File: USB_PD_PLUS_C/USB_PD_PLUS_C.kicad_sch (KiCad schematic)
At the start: 28 parts, among them J1 USB3_A, U1 NDP1360KC, U3 CH482D, U4 CXP0650-220M-AG(22UH), U5 LM317L_SOT-89

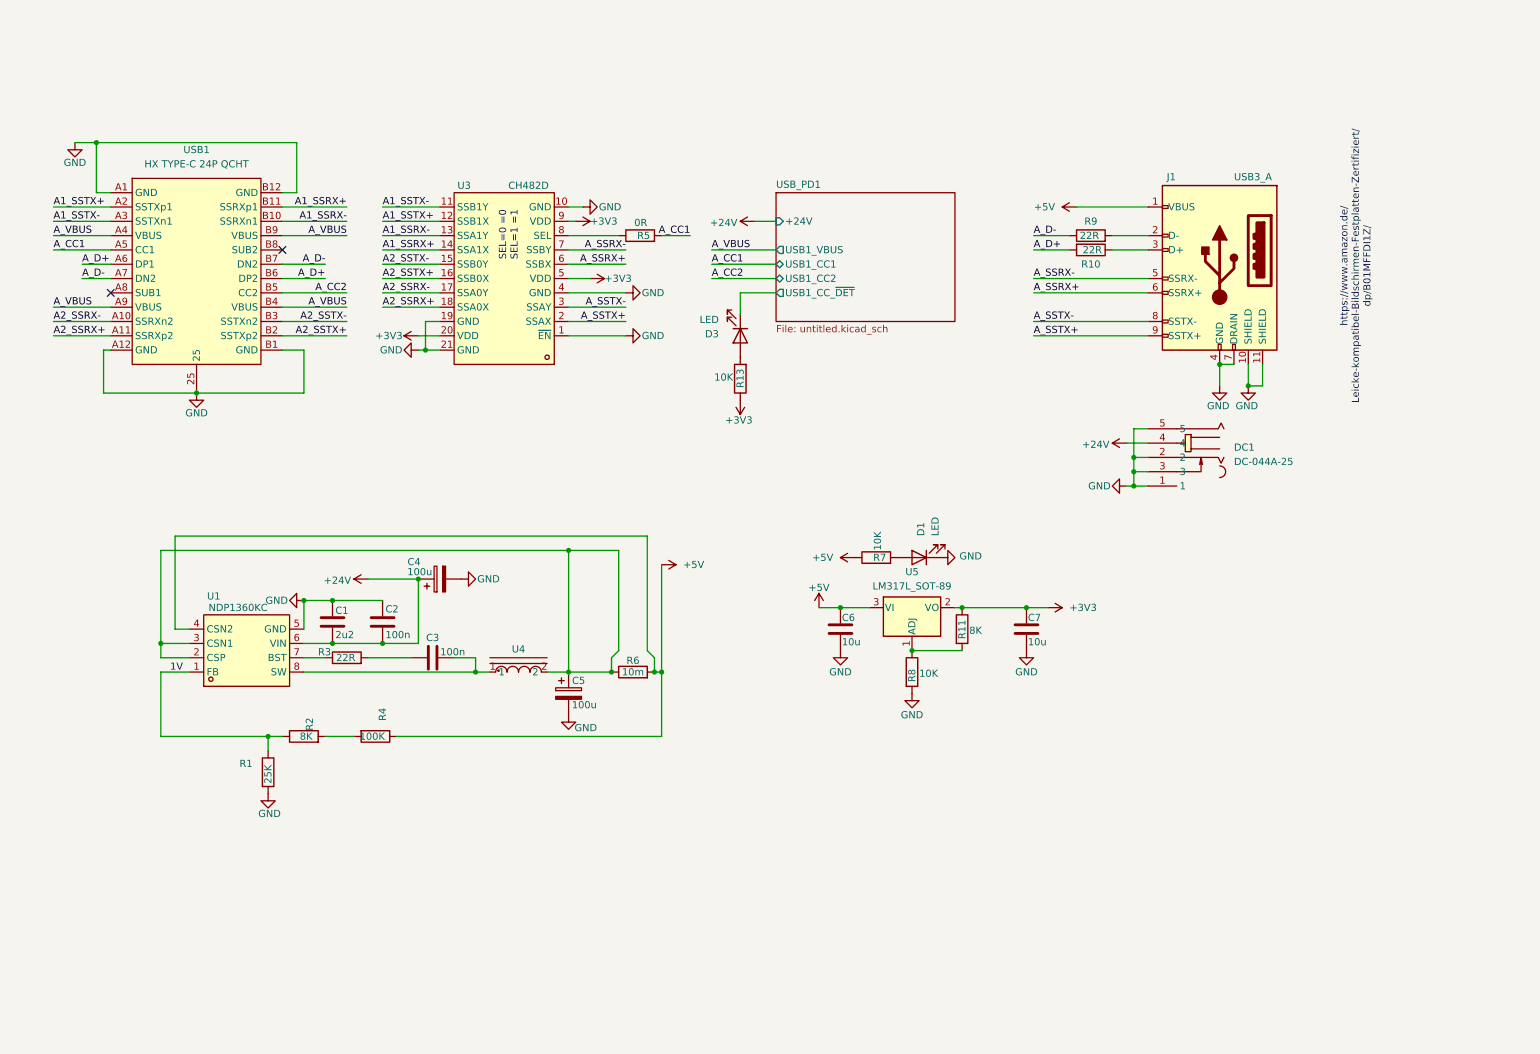
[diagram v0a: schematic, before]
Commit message: Update Schematic to 3 Port USB-C Power
I updated the schamtic to 3 port usb-C with superspeed and PD working
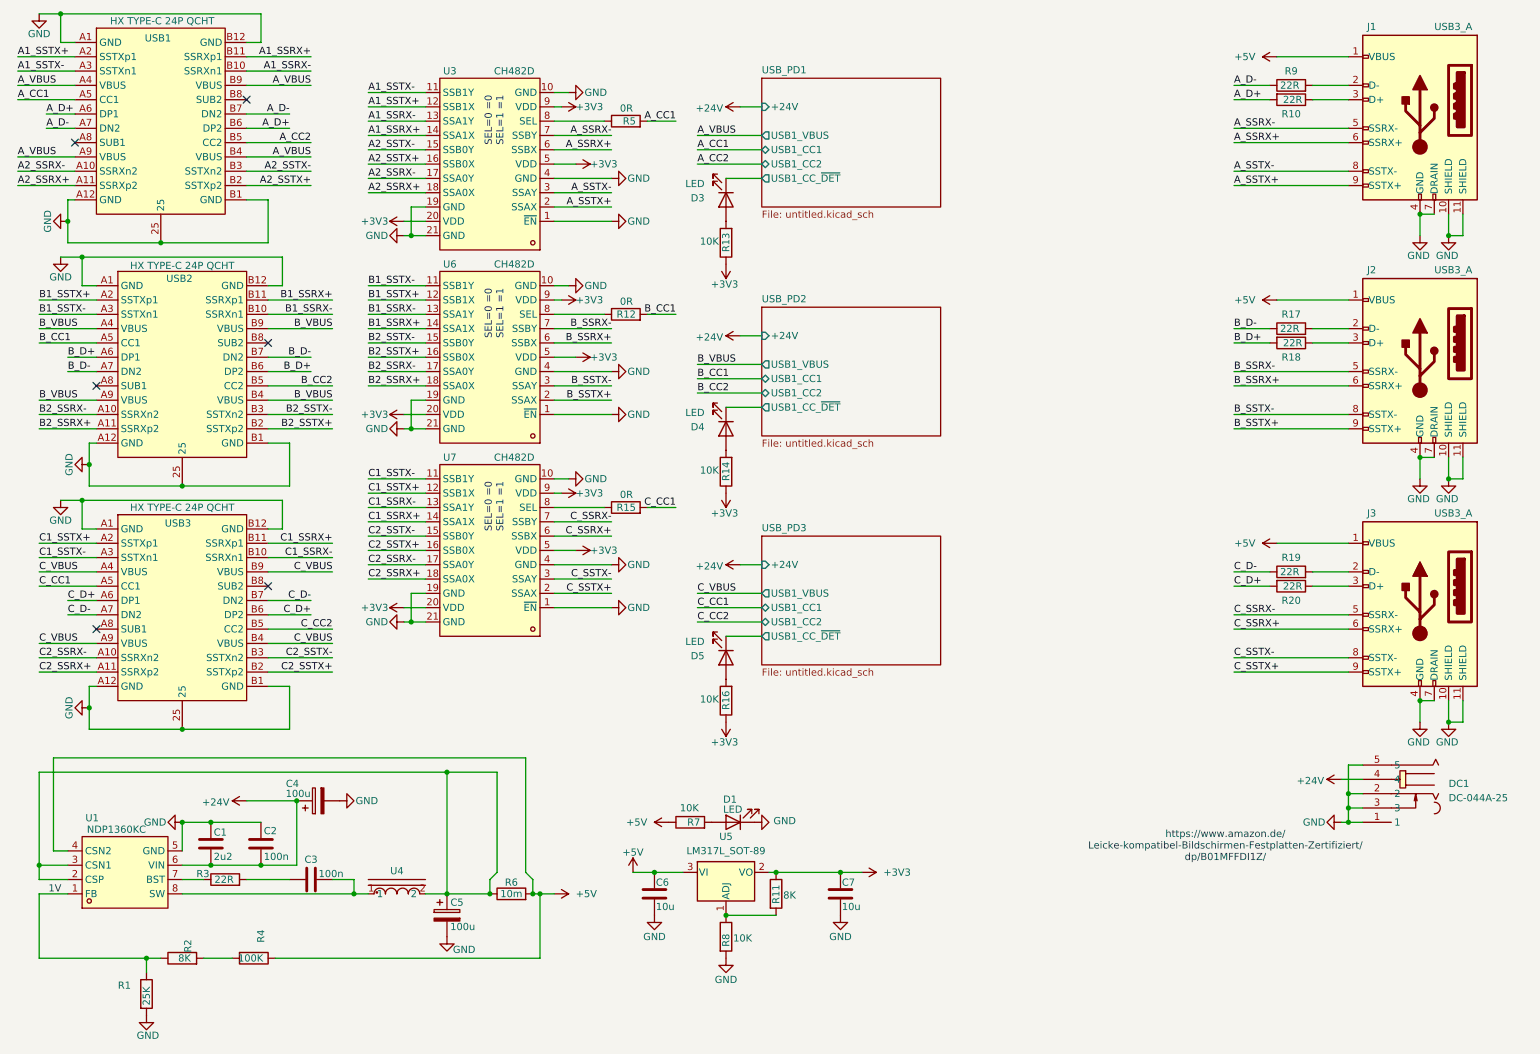
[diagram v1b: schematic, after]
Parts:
- added D4, D5: LED, LED_SMD:LED_0603_1608Metric, symbol Device:LED
- added J2, J3: USB3_A, easyeda2kicad:USB-3.0-A-TH_HC-ST-003-01-Z, symbol Connector:USB3_A
- added R12, R15: 0R, Resistor_SMD:R_0402_1005Metric, symbol Device:R
- added R14, R16: 10K, Resistor_SMD:R_0402_1005Metric, symbol Device:R
- added R17, R18, R19, R20: 22R, Resistor_SMD:R_0402_1005Metric, symbol Device:R
- added U6, U7: CH482D, easyeda2kicad:VFQFN-20_L4.5-W2.5-P0.5-BL-EP, symbol EASYEDA:CH482D
- added USB2, USB3: HX TYPE-C 24P QCHT, easyeda2kicad:TYPE-C-SMD_TYPE-C-24P-QCHT, symbol EASYEDA:HXTYPE-C24PQCHT
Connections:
- net +3V3: now also R14.1, R16.1, U6.20 (VDD), U6.5 (VDD), U6.9 (VDD), U7.20 (VDD), U7.5 (VDD), U7.9 (VDD)
- net +5V: now also J2.1 (VBUS), J3.1 (VBUS)
- net GND: now also J2.10 (SHIELD), J2.11 (SHIELD), J2.4 (GND), J2.7 (DRAIN), J3.10 (SHIELD), J3.11 (SHIELD), J3.4 (GND), J3.7 (DRAIN), U6.1 (~{EN}), U6.10 (GND), U6.19 (GND), U6.21 (GND), U6.4 (GND), U7.1 (~{EN}), U7.10 (GND), U7.19 (GND), U7.21 (GND), U7.4 (GND), USB2.25, USB2.A1 (GND), USB2.A12 (GND), USB2.B1 (GND), USB2.B12 (GND), USB3.25, USB3.A1 (GND), USB3.A12 (GND), USB3.B1 (GND), USB3.B12 (GND)
- new net: R15.1, U7.8 (SEL)
- new net: D5.2 (A), R16.2
- new net: R12.1, U6.8 (SEL)
- new net: J2.3 (D+), R18.1
- new net: D4.2 (A), R14.2
- new net: J3.2 (D-), R19.2
- new net: J3.3 (D+), R20.1
- new net: J2.2 (D-), R17.2
- new net B1_SSRX+: U6.14 (SSA1X), USB2.B11 (SSRXp1)
- new net B1_SSRX-: U6.13 (SSA1Y), USB2.B10 (SSRXn1)
- new net B1_SSTX+: U6.12 (SSB1X), USB2.A2 (SSTXp1)
- new net B1_SSTX-: U6.11 (SSB1Y), USB2.A3 (SSTXn1)
- new net B2_SSRX+: U6.18 (SSA0X), USB2.A11 (SSRXp2)
- new net B2_SSRX-: U6.17 (SSA0Y), USB2.A10 (SSRXn2)
- new net B2_SSTX+: U6.16 (SSB0X), USB2.B2 (SSTXp2)
- new net B2_SSTX-: U6.15 (SSB0Y), USB2.B3 (SSTXn2)
- new net B_CC1: R12.2, USB2.A5 (CC1)
- new net B_CC2: USB2.B5 (CC2)
- new net B_D+: R18.2, USB2.A6 (DP1), USB2.B6 (DP2)
- new net B_D-: R17.1, USB2.A7 (DN2), USB2.B7 (DN2)
- new net B_SSRX+: J2.6 (SSRX+), U6.6 (SSBX)
- new net B_SSRX-: J2.5 (SSRX-), U6.7 (SSBY)
- new net B_SSTX+: J2.9 (SSTX+), U6.2 (SSAX)
- new net B_SSTX-: J2.8 (SSTX-), U6.3 (SSAY)
- new net B_VBUS: USB2.A4 (VBUS), USB2.A9 (VBUS), USB2.B4 (VBUS), USB2.B9 (VBUS)
- new net C1_SSRX+: U7.14 (SSA1X), USB3.B11 (SSRXp1)
- new net C1_SSRX-: U7.13 (SSA1Y), USB3.B10 (SSRXn1)
- new net C1_SSTX+: U7.12 (SSB1X), USB3.A2 (SSTXp1)
- new net C1_SSTX-: U7.11 (SSB1Y), USB3.A3 (SSTXn1)
- new net C2_SSRX+: U7.18 (SSA0X), USB3.A11 (SSRXp2)
- new net C2_SSRX-: U7.17 (SSA0Y), USB3.A10 (SSRXn2)
- new net C2_SSTX+: U7.16 (SSB0X), USB3.B2 (SSTXp2)
- new net C2_SSTX-: U7.15 (SSB0Y), USB3.B3 (SSTXn2)
- new net C_CC1: R15.2, USB3.A5 (CC1)
- new net C_CC2: USB3.B5 (CC2)
- new net C_D+: R20.2, USB3.A6 (DP1), USB3.B6 (DP2)
- new net C_D-: R19.1, USB3.A7 (DN2), USB3.B7 (DN2)
- new net C_SSRX+: J3.6 (SSRX+), U7.6 (SSBX)
- new net C_SSRX-: J3.5 (SSRX-), U7.7 (SSBY)
- new net C_SSTX+: J3.9 (SSTX+), U7.2 (SSAX)
- new net C_SSTX-: J3.8 (SSTX-), U7.3 (SSAY)
- new net C_VBUS: USB3.A4 (VBUS), USB3.A9 (VBUS), USB3.B4 (VBUS), USB3.B9 (VBUS)
- new net USB_PD2/USB1_CC_~{DET}: D4.1 (K)
- new net USB_PD3/USB1_CC_~{DET}: D5.1 (K)
- no-connect marks 2 -> 6
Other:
- added sheet USB_PD2 (untitled.kicad_sch)
- added sheet USB_PD3 (untitled.kicad_sch)
- moved on the sheet: C1, C2, C3, C4, C5, C6, C7, D1, D3, DC1, J1, R1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

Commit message: update USB PD PCB to 3 in 3 out
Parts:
- removed C1: 2u2, easyeda2kicad:C1812, symbol Device:C
- removed C4, C5: 100u, Capacitor_SMD:CP_Elec_8x10, symbol Device:C_Polarized
- added C16, C9: 22u, easyeda2kicad:C1812, symbol Device:C
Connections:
- net +24V: now also C16.1
- net GND: now also C16.2, C9.2
- net at R6.1, U1.2 (CSP), U1.3 (CSN1)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: now also C9.1
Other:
- moved on the sheet: C2

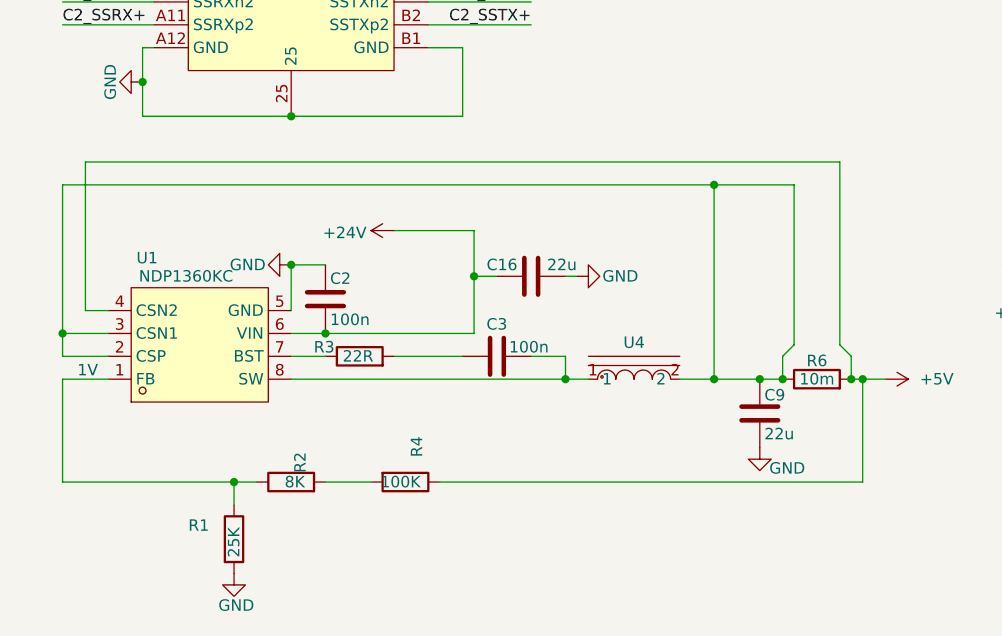
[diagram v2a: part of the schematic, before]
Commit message: update routing usb c pd
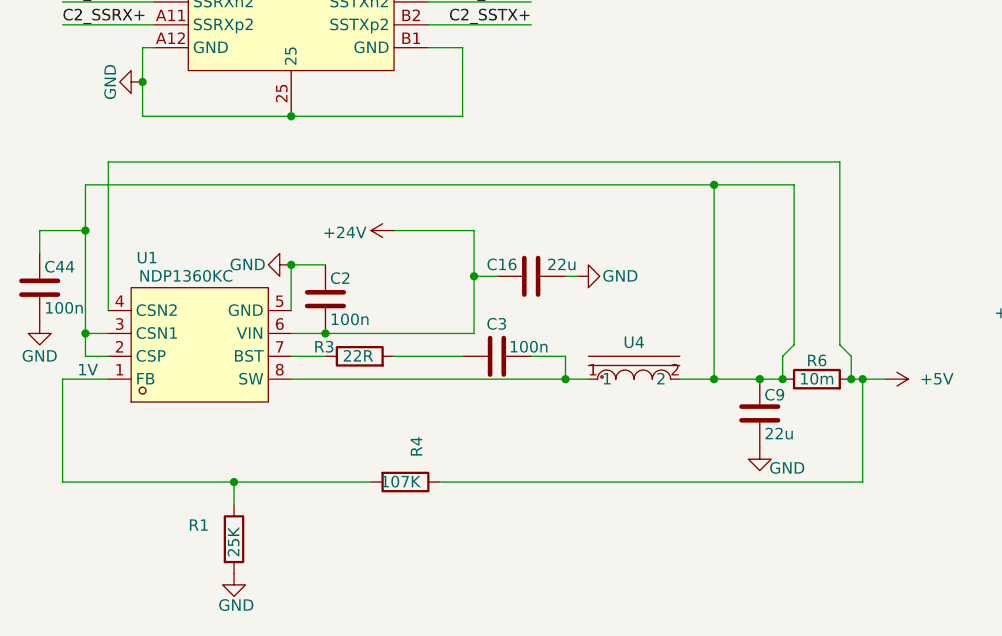
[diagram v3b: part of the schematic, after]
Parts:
- removed R2: 8K, Resistor_SMD:R_0402_1005Metric, symbol Device:R
- added C44: 100n, Capacitor_SMD:C_0402_1005Metric, symbol Device:C
- C2, C3: footprint Capacitor_SMD:C_0603_1608Metric -> Capacitor_SMD:C_0402_1005Metric; LCSC C5137636 -> C5142567
- R4: value 100K -> 107K; LCSC Part C3017514 -> C25743
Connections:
- net GND: now also C44.2
- net at R1.1, U1.1 (FB): now also R4.2
- net at C9.1, R6.1, U1.2 (CSP)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: now also C44.1

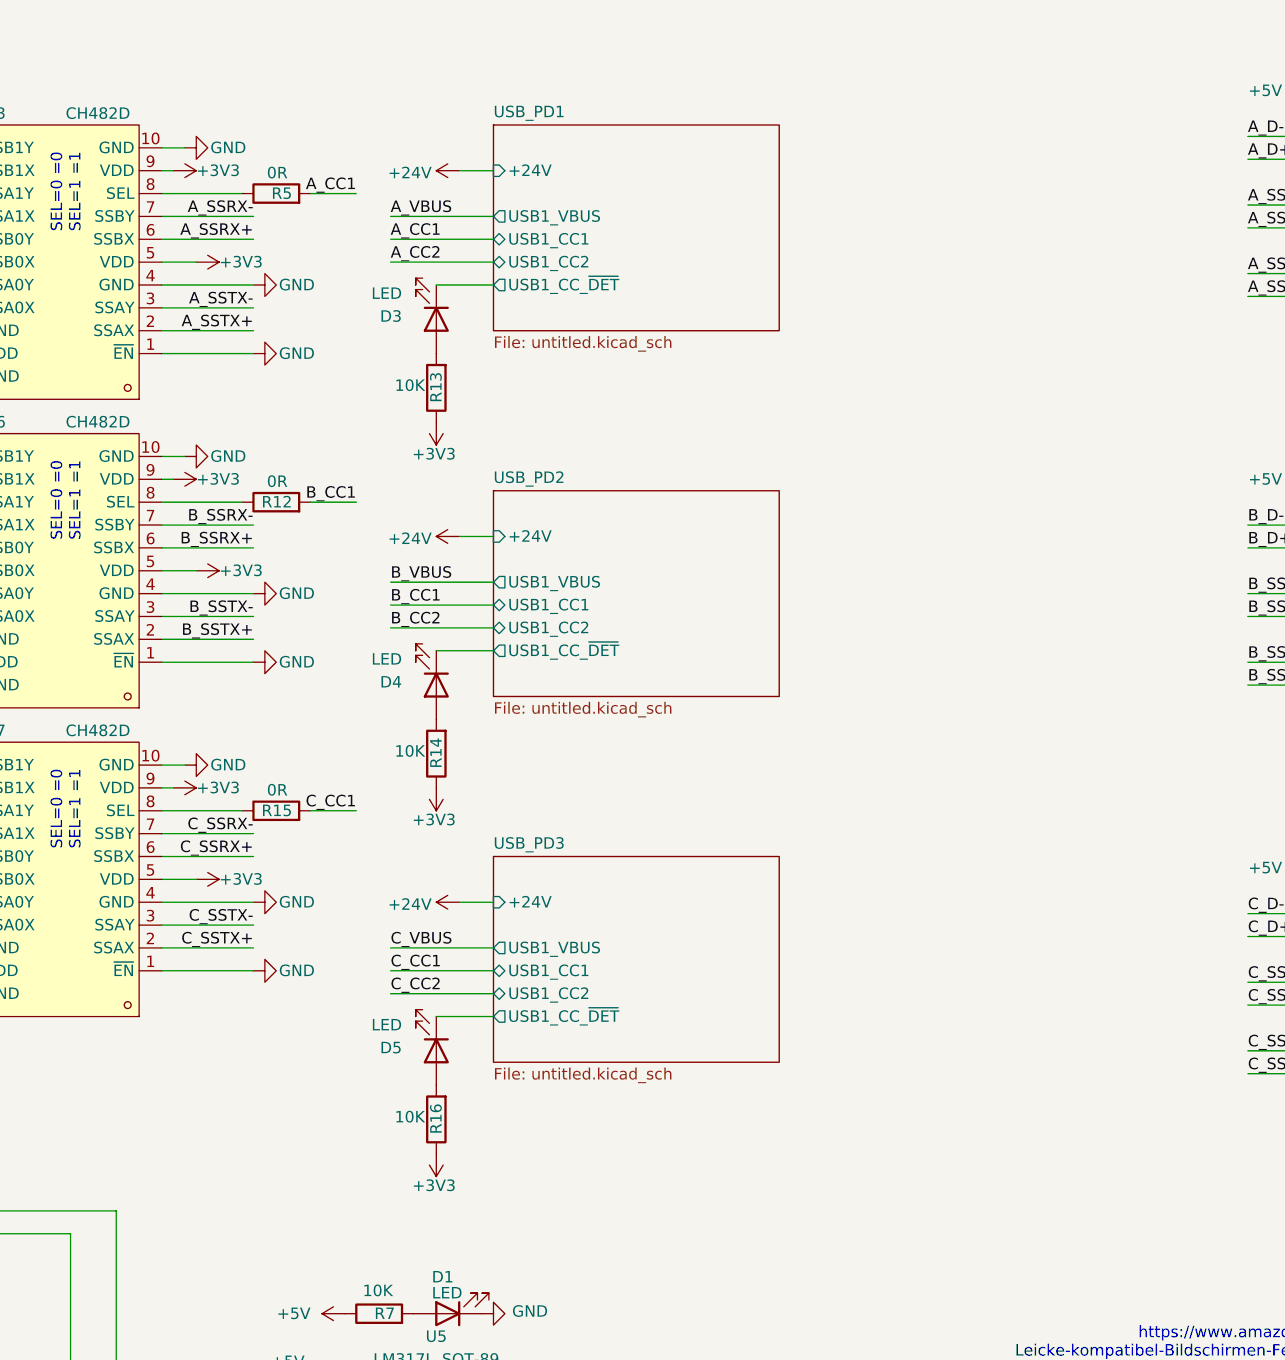
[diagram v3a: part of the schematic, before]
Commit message: CC Bug
there was a error, to detect cable orientation. now it should work
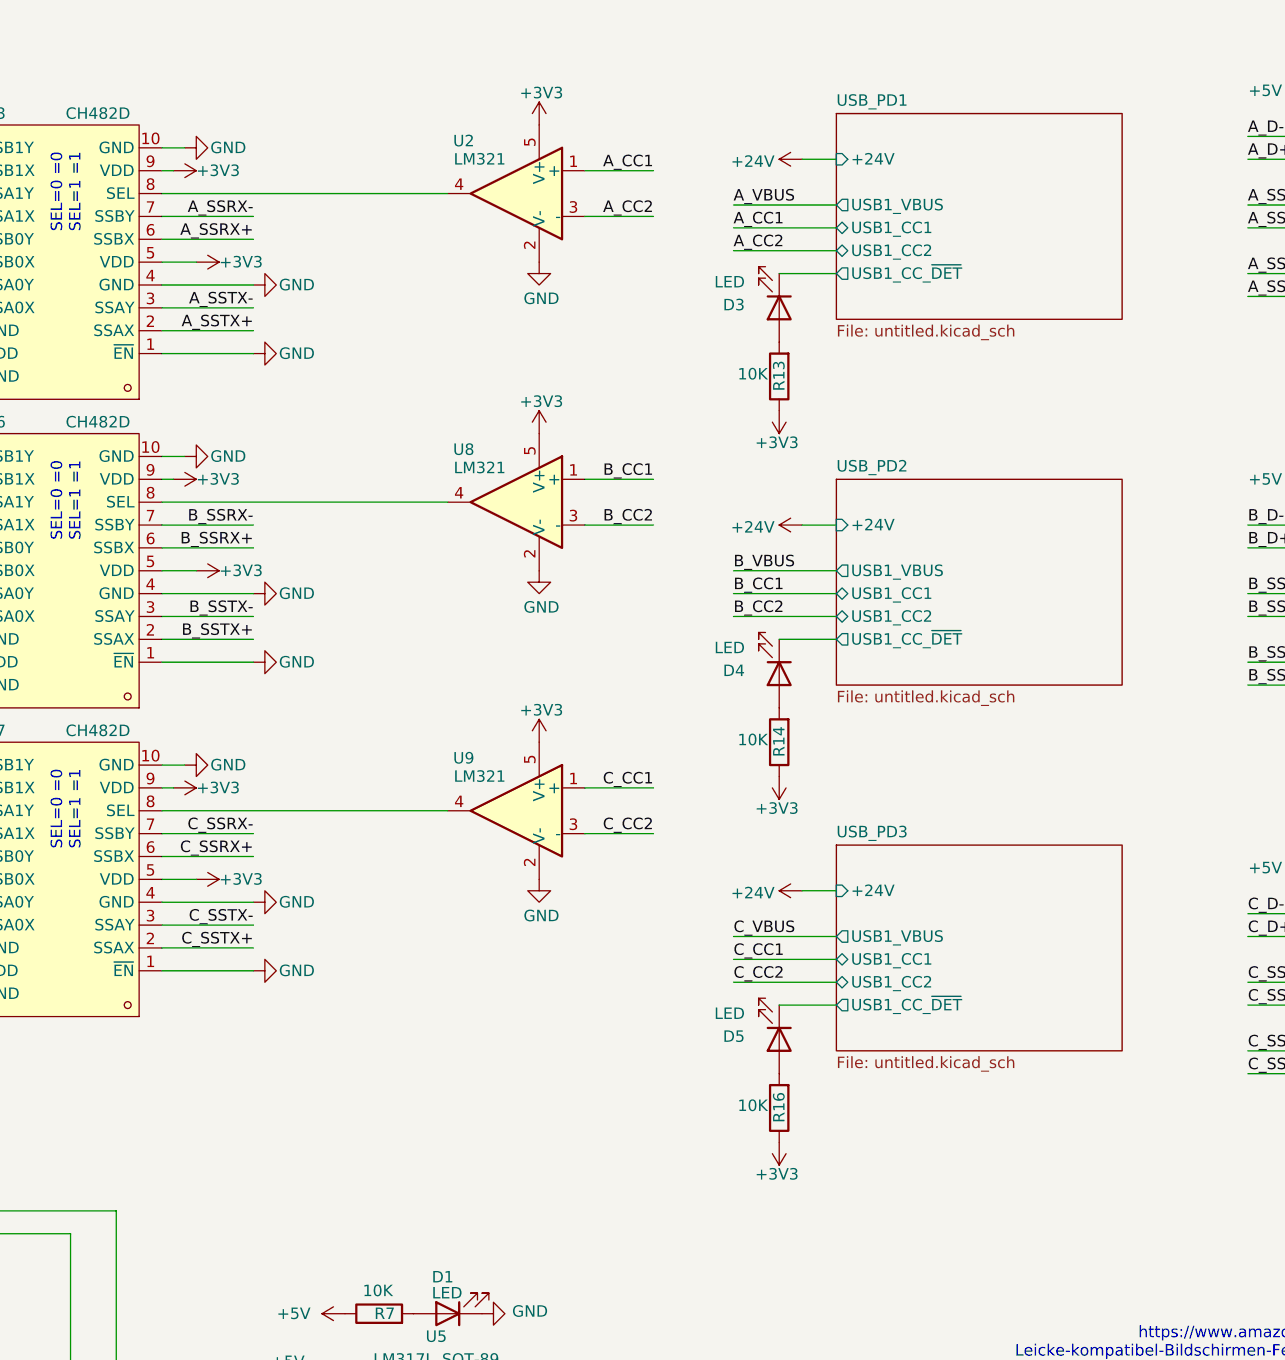
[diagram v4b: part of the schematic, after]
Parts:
- removed R12, R15, R5: 0R, Resistor_SMD:R_0402_1005Metric, symbol Device:R
- added U2, U8, U9: LM321, Package_TO_SOT_SMD:SOT-23-5, symbol Amplifier_Operational:LM321
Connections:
- net +3V3: now also U2.5 (V+), U8.5 (V+), U9.5 (V+)
- net A_CC1: now also U2.1 (+)
- net A_CC2: now also U2.3 (-)
- net B_CC1: now also U8.1 (+)
- net B_CC2: now also U8.3 (-)
- net C_CC1: now also U9.1 (+)
- net C_CC2: now also U9.3 (-)
- net GND: now also U2.2 (V-), U8.2 (V-), U9.2 (V-)
- net at U7.8 (SEL): now also U9.4
- net at U3.8 (SEL): now also U2.4
- net at U6.8 (SEL): now also U8.4
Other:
- moved on the sheet: D3, D4, D5, R13, R14, R16
